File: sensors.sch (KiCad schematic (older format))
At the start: 13 parts

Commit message: Update schematic labels to handle hierarchical signal dependencies
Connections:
- wire segments 42 -> 48
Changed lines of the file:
@@
 	1    0    0    -1
 $EndComp
-Text Label 3750 1950 0    39   ~ 0
-SPI1_MISO
-Text Label 3750 2100 0    39   ~ 0
-SPI1_NSS
-Text Label 3750 1800 0    39   ~ 0
-SPI1_MOSI
-Text Label 3750 1700 0    39   ~ 0
-SPI1_SCK
 NoConn ~ 3700 1450
 NoConn ~ 3700 1550
 NoConn ~ 3700 2450
-Text Label 3750 2250 0    39   ~ 0
-MPU9250_INT
 $Comp
 L MPU-9250 U?
@@
 	1    0    0    -1
 $EndComp
-Text Label 5900 1600 2    39   ~ 0
-+2.8V
-Text Label 5900 2150 2    39   ~ 0
-+2.8V
 Wire Wire Line
 	2100 2800 1900 2800
@@
 	1900 2800 1900 2850
 Wire Wire Line
-	1650 1450 2100 1450
+	1650 1450 2050 1450
+Wire Wire Line
+	2050 1450 2100 1450
 Wire Wire Line
 	1650 1750 2100 1750
@@
 	3700 2700 3850 2700
 Wire Wire Line
-	5900 1600 6200 1600
-Wire Wire Line
-	5900 2150 6200 2150
+	5900 1600 6050 1600
+Wire Wire Line
+	6050 1600 6200 1600
+Wire Wire Line
+	5900 2150 6050 2150
+Wire Wire Line
+	6050 2150 6200 2150
 $Comp
 L C C?
@@
 	1    0    0    -1
 $EndComp
-Text Label 7950 1150 0    39   ~ 0
-+2.8V
-Wire Wire Line
-	7700 1150 7950 1150
+Wire Wire Line
+	7700 1150 7850 1150
+Wire Wire Line
+	7850 1150 7950 1150
 Wire Wire Line
 	7850 1150 7850 1250
@@
 Wire Wire Line
 	7850 1700 7850 1550
-Text Label 9300 1050 0    39   ~ 0
-+2.8V
 $Comp
 L R R?
@@
 	9200 1400 9200 1050
 Wire Wire Line
-	9050 1050 9300 1050
+	9050 1050 9200 1050
+Wire Wire Line
+	9200 1050 9300 1050
 Wire Wire Line
 	9050 1050 9050 1100
@@
 	10150 1600 10150 1550
 Wire Wire Line
-	10150 1550 10400 1550
+	10150 1550 10300 1550
+Wire Wire Line
+	10300 1550 10400 1550
 Wire Wire Line
 	10300 1550 10300 1900
@@
 Connection ~ 10150 2200
 Connection ~ 10300 1550
-Text Label 10400 1550 0    39   ~ 0
-+2.8V
-Text Label 9500 1700 0    39   ~ 0
+Wire Wire Line
+	9500 1700 9450 1700
+Wire Wire Line
+	10600 2200 10550 2200
+Text HLabel 3750 1700 2    39   Input ~ 0
+SPI1_SCK
+Text HLabel 3750 1800 2    39   Input ~ 0
+SPI1_MOSI
+Text HLabel 3750 1950 2    39   Input ~ 0
+SPI1_MISO
+Text HLabel 3750 2100 2    39   Input ~ 0
+SPI1_NSS
+Text HLabel 3750 2250 2    39   Input ~ 0
+MPU9250_INT
+Text HLabel 5900 1600 0    39   Input ~ 0
++2.8V
+Text HLabel 5900 2150 0    39   Input ~ 0
++2.8V
+Text HLabel 7950 1150 2    39   Input ~ 0
++2.8V
+Text HLabel 9300 1050 2    39   Input ~ 0
++2.8V
+Text HLabel 10400 1550 2    39   Input ~ 0
++2.8V
+Text HLabel 10600 2200 2    39   Input ~ 0
+I2C1_SDA
+Text HLabel 9500 1700 2    39   Input ~ 0
 I2C1_SCL
-Wire Wire Line
-	9500 1700 9450 1700
-Text Label 10600 2200 0    39   ~ 0
-I2C1_SDA
-Wire Wire Line
-	10600 2200 10550 2200
 $EndSCHEMATC

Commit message: Add principal power supply
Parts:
- removed Q? (x2): BSS138, SOT-23, symbol BSS138
- removed R? (x2): 2.2k, symbol R
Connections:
- net labels removed: +2.8V, I2C1_SCL_2.8V, I2C1_SDA_2.8V
- wire segments 48 -> 32
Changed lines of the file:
@@
 	1900 2800 1900 2850
 Wire Wire Line
-	1650 1450 2050 1450
-Wire Wire Line
-	2050 1450 2100 1450
+	1650 1450 2100 1450
 Wire Wire Line
 	1650 1750 2100 1750
@@
 	3700 2700 3850 2700
 Wire Wire Line
-	5900 1600 6050 1600
+	5900 1600 6200 1600
 Wire Wire Line
-	6050 1600 6200 1600
-Wire Wire Line
-	5900 2150 6050 2150
-Wire Wire Line
-	6050 2150 6200 2150
+	5900 2150 6200 2150
 $Comp
 L C C?
@@
 	7700 1150 7850 1150
 Wire Wire Line
-	7850 1150 7950 1150
-Wire Wire Line
-	7850 1150 7850 1250
+	7850 1100 7850 1250
 Wire Wire Line
 	7700 1150 7700 1250
@@
 Wire Wire Line
 	7850 1700 7850 1550
-$Comp
-L R R?
-U 1 1 5536FF70
-P 10150 1750
-F 0 "R?" V 10230 1750 50  0000 C CNN
-F 1 "2.2k" V 10150 1750 50  0000 C CNN
-F 2 "" V 10080 1750 30  0000 C CNN
-F 3 "" H 10150 1750 30  0000 C CNN
-	1    10150 1750
-	1    0    0    -1
-$EndComp
 Wire Wire Line
 	7650 1850 7700 1850
@@
 	7700 1600 7700 1550
 Text Label 7700 1850 0    39   ~ 0
-I2C1_SCL_2.8V
+I2C1_SCL
 Text Label 7700 1950 0    39   ~ 0
-I2C1_SDA_2.8V
+I2C1_SDA
 $Comp
 L VL6180X U?
@@
 	1    0    0    -1
 $EndComp
-$Comp
-L R R?
-U 1 1 5536FEA0
-P 9050 1250
-F 0 "R?" V 9130 1250 50  0000 C CNN
-F 1 "2.2k" V 9050 1250 50  0000 C CNN
-F 2 "" V 8980 1250 30  0000 C CNN
-F 3 "" H 9050 1250 30  0000 C CNN
-	1    9050 1250
-	1    0    0    -1
-$EndComp
-$Comp
-L BSS138 Q?
-U 1 1 5537886E
-P 9250 1600
-F 0 "Q?" H 9450 1675 50  0000 L CNN
-F 1 "BSS138" H 9450 1600 50  0000 L CNN
-F 2 "SOT-23" H 9450 1525 50  0000 L CIN
-F 3 "" H 9250 1600 50  0000 L CNN
-	1    9250 1600
-	0    1    1    0
-$EndComp
-$Comp
-L BSS138 Q?
-U 1 1 553788BF
-P 10350 2100
-F 0 "Q?" H 10550 2175 50  0000 L CNN
-F 1 "BSS138" H 10550 2100 50  0000 L CNN
-F 2 "SOT-23" H 10550 2025 50  0000 L CIN
-F 3 "" H 10350 2100 50  0000 L CNN
-	1    10350 2100
-	0    1    1    0
-$EndComp
-Text Label 9000 1700 2    39   ~ 0
-I2C1_SCL_2.8V
-Text Label 10100 2200 2    39   ~ 0
-I2C1_SDA_2.8V
-Wire Wire Line
-	9000 1700 9050 1700
-Wire Wire Line
-	10100 2200 10150 2200
-Wire Wire Line
-	9050 1700 9050 1400
-Connection ~ 9050 1700
-Wire Wire Line
-	9200 1400 9200 1050
-Wire Wire Line
-	9050 1050 9200 1050
-Wire Wire Line
-	9200 1050 9300 1050
-Wire Wire Line
-	9050 1050 9050 1100
-Connection ~ 9200 1050
-Wire Wire Line
-	10150 1600 10150 1550
-Wire Wire Line
-	10150 1550 10300 1550
-Wire Wire Line
-	10300 1550 10400 1550
-Wire Wire Line
-	10300 1550 10300 1900
-Wire Wire Line
-	10150 2200 10150 1900
-Connection ~ 10150 2200
-Connection ~ 10300 1550
-Wire Wire Line
-	9500 1700 9450 1700
-Wire Wire Line
-	10600 2200 10550 2200
 Text HLabel 3750 1700 2    39   Input ~ 0
 SPI1_SCK
@@
 Text HLabel 3750 2250 2    39   Input ~ 0
 MPU9250_INT
-Text HLabel 5900 1600 0    39   Input ~ 0
-+2.8V
-Text HLabel 5900 2150 0    39   Input ~ 0
-+2.8V
-Text HLabel 7950 1150 2    39   Input ~ 0
-+2.8V
-Text HLabel 9300 1050 2    39   Input ~ 0
-+2.8V
-Text HLabel 10400 1550 2    39   Input ~ 0
-+2.8V
-Text HLabel 10600 2200 2    39   Input ~ 0
-I2C1_SDA
-Text HLabel 9500 1700 2    39   Input ~ 0
-I2C1_SCL
+$Comp
+L VCC #PWR?
+U 1 1 55382F10
+P 7850 1100
+F 0 "#PWR?" H 7850 950 50  0001 C CNN
+F 1 "VCC" H 7850 1250 50  0000 C CNN
+F 2 "" H 7850 1100 60  0000 C CNN
+F 3 "" H 7850 1100 60  0000 C CNN
+	1    7850 1100
+	1    0    0    -1
+$EndComp
+$Comp
+L VCC #PWR?
+U 1 1 55382F46
+P 5900 1550
+F 0 "#PWR?" H 5900 1400 50  0001 C CNN
+F 1 "VCC" H 5900 1700 50  0000 C CNN
+F 2 "" H 5900 1550 60  0000 C CNN
+F 3 "" H 5900 1550 60  0000 C CNN
+	1    5900 1550
+	1    0    0    -1
+$EndComp
+$Comp
+L VCC #PWR?
+U 1 1 55382F63
+P 5900 2100
+F 0 "#PWR?" H 5900 1950 50  0001 C CNN
+F 1 "VCC" H 5900 2250 50  0000 C CNN
+F 2 "" H 5900 2100 60  0000 C CNN
+F 3 "" H 5900 2100 60  0000 C CNN
+	1    5900 2100
+	1    0    0    -1
+$EndComp
+Wire Wire Line
+	5900 2100 5900 2150
+Wire Wire Line
+	5900 1550 5900 1600
 $EndSCHEMATC

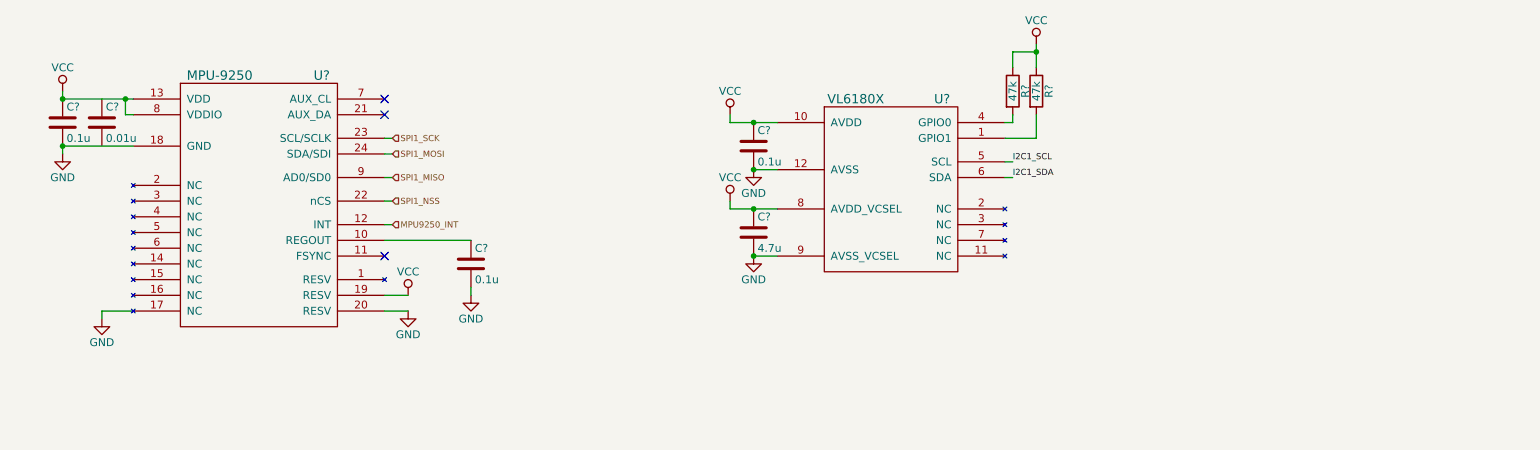
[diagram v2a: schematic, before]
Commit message: Barometer in schematic
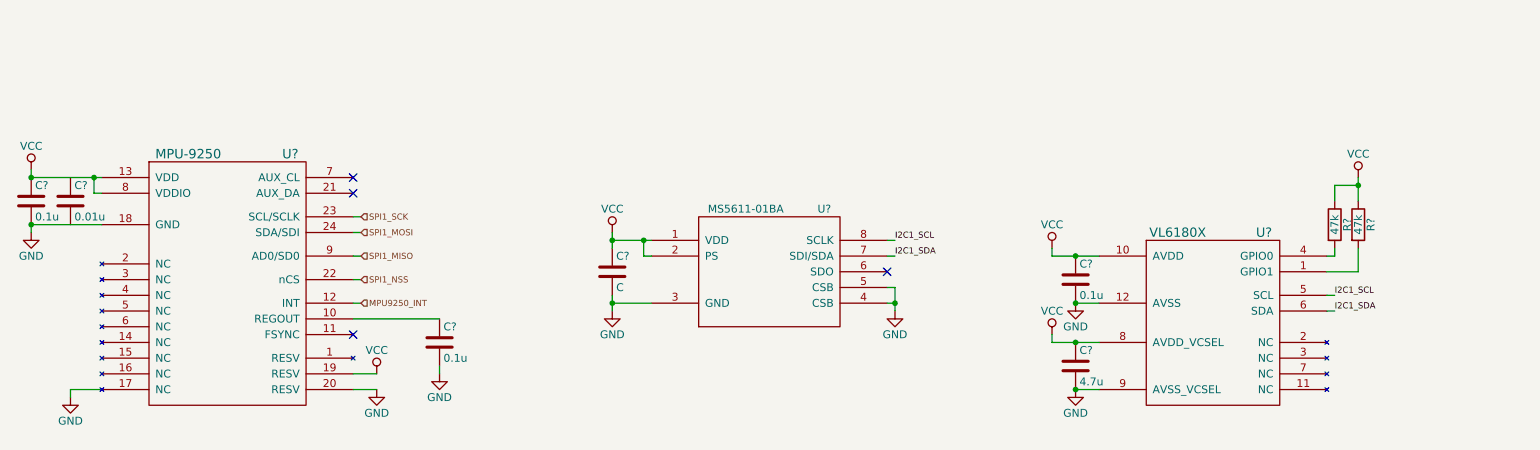
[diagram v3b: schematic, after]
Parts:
- added C?: C, symbol C
- added U?: MS5611-01BA, MODULE, symbol MS5611-01BA
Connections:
- net GND: now also C?.2, U?.3 (GND), U?.4 (CSB), U?.5 (CSB)
- net I2C1_SCL: now also U?.8 (SCLK)
- net I2C1_SDA: now also U?.7 (SDI/SDA)
- net VCC: now also C?.1, U?.1 (VDD), U?.2 (PS)
- no-connect marks 3 -> 4
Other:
- moved on the sheet: C?, R?, U?

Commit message: CAN transceiver added in schematics
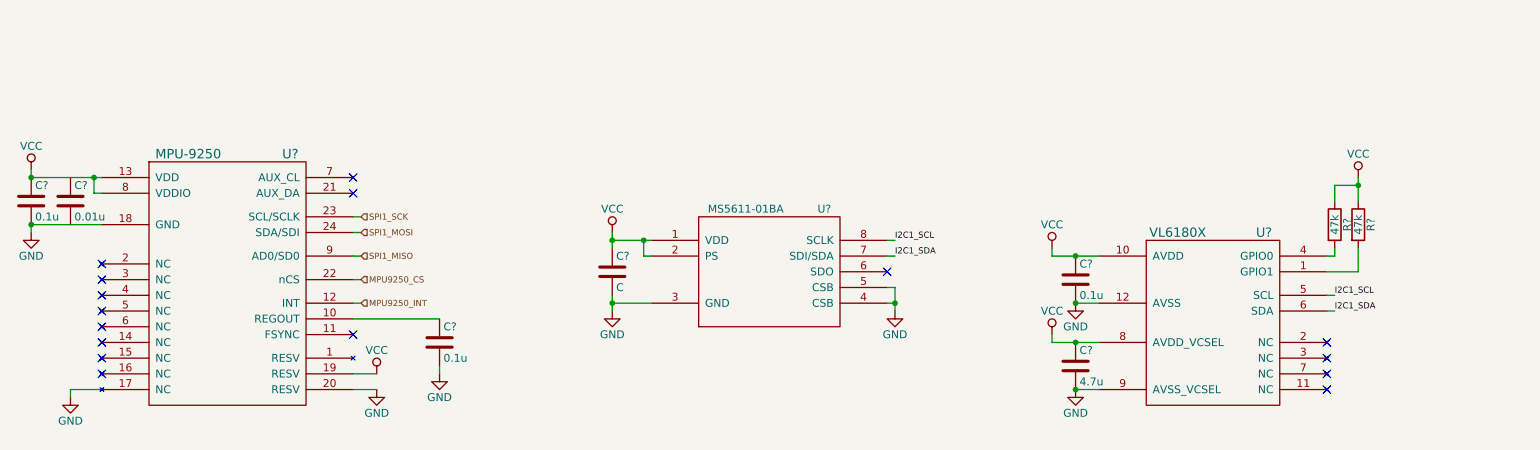
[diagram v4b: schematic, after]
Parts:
- removed U?: MPU-9250, symbol MPU-9250
- added U?: MPU-9250, symbol MPU-9250
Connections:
- net GND: now also U?.17 (NC), U?.18 (GND), U?.20 (RESV)
- net MPU9250_INT: now also U?.12 (INT)
- net SPI1_MISO: now also U?.9 (AD0/SD0)
- net SPI1_MOSI: now also U?.24 (SDA/SDI)
- net SPI1_SCK: now also U?.23 (SCL/SCLK)
- net VCC: now also U?.13 (VDD), U?.19 (RESV), U?.8 (VDDIO)
- net at C?.1: now also U?.10 (REGOUT)
- new net MPU9250_CS: U?.22 (nCS)
- no-connect marks 4 -> 16
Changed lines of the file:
@@
 NoConn ~ 3500 2950
-$Comp
-L MPU-9250 U?
-U 1 1 5536DEAA
-P 2700 2600
-F 0 "U?" H 3100 3400 60  0000 C CNN
-F 1 "MPU-9250" H 2450 3400 60  0000 C CNN
-F 2 "" H 2700 3200 60  0000 C CNN
-F 3 "" H 2700 3200 60  0000 C CNN
-	1    2700 2600
-	1    0    0    -1
-$EndComp
 $Comp
 L VCC #PWR?
@@
 SPI1_MISO
 Text HLabel 3550 2600 2    39   Input ~ 0
-SPI1_NSS
+MPU9250_CS
 Text HLabel 3550 2750 2    39   Input ~ 0
 MPU9250_INT
@@
 	6950 2650 6900 2650
 Connection ~ 6950 2750
+NoConn ~ 9700 3000
+NoConn ~ 9700 3100
+NoConn ~ 9700 3200
+NoConn ~ 9700 3300
+NoConn ~ 1900 3200
+NoConn ~ 1900 3100
+NoConn ~ 1900 3000
+NoConn ~ 1900 2900
+NoConn ~ 1900 2800
+NoConn ~ 1900 2700
+NoConn ~ 1900 2600
+NoConn ~ 1900 2500
+$Comp
+L MPU-9250 U?
+U 1 1 553B9407
+P 2700 2600
+F 0 "U?" H 3100 3400 60  0000 C CNN
+F 1 "MPU-9250" H 2450 3400 60  0000 C CNN
+F 2 "" H 2700 3200 60  0000 C CNN
+F 3 "" H 2700 3200 60  0000 C CNN
+	1    2700 2600
+	1    0    0    -1
+$EndComp
 $EndSCHEMATC

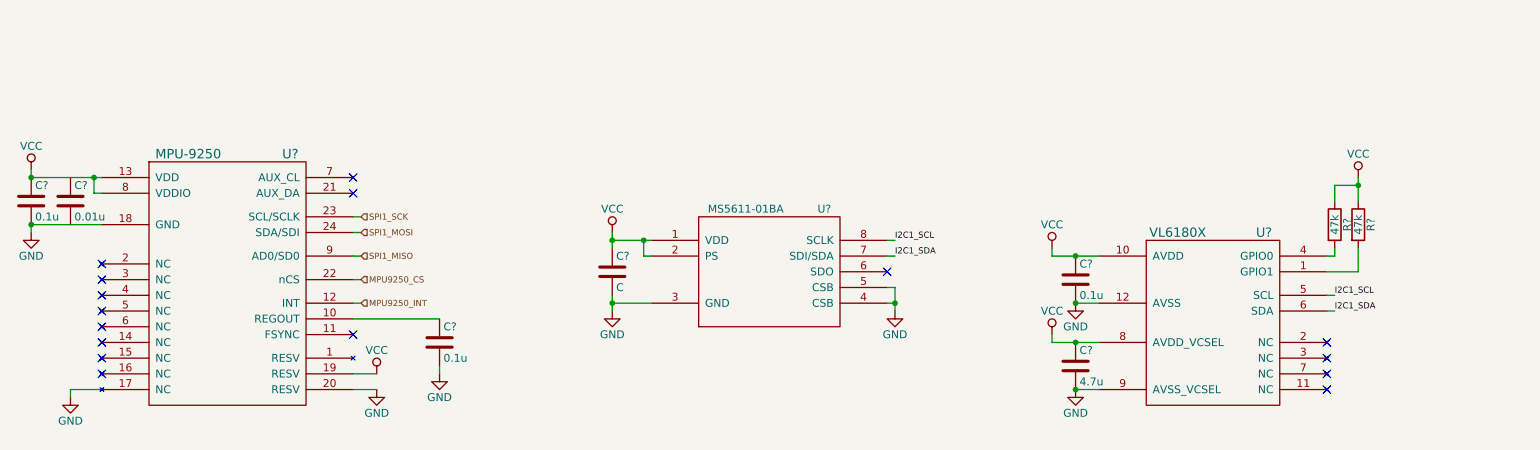
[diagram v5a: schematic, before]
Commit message: nRF24L01+ integrated + correct capacitors
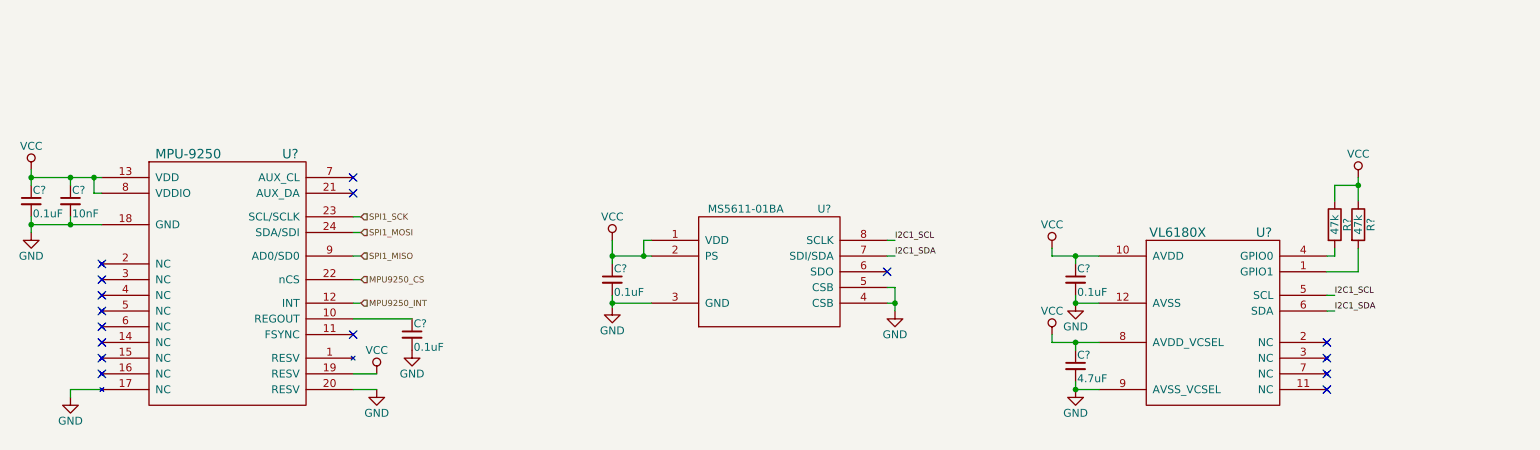
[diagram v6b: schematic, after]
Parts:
- removed C? (x3): 0.1u, symbol C
- removed C?: 0.01u, symbol C
- removed C?: 4.7u, symbol C
- removed C?: C, symbol C
- added C? (x4): 0.1uF, symbol C_Small
- added C?: 10nF, symbol C_Small
- added C?: 4.7uF, symbol C_Small
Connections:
- net GND: now also C?.2, C?.2, C?.2, C?.2, C?.2, C?.2
- net VCC: now also C?.1, C?.1, C?.1, C?.1, C?.1
- net at U?.10 (REGOUT): now also C?.1
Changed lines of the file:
@@
-$EndComp
-$Comp
-L C C?
-U 1 1 5536D1BC
-P 1450 2100
-F 0 "C?" H 1475 2200 50  0000 L CNN
-F 1 "0.1u" H 1475 2000 50  0000 L CNN
-F 2 "" H 1488 1950 30  0000 C CNN
-F 3 "" H 1450 2100 60  0000 C CNN
-	1    1450 2100
-	1    0    0    -1
 $EndComp
 $Comp
@@
 $EndComp
 $Comp
-L C C?
-U 1 1 5536D8E2
-P 1700 2100
-F 0 "C?" H 1725 2200 50  0000 L CNN
-F 1 "0.01u" H 1725 2000 50  0000 L CNN
-F 2 "" H 1738 1950 30  0000 C CNN
-F 3 "" H 1700 2100 60  0000 C CNN
-	1    1700 2100
-	1    0    0    -1
-$EndComp
-$Comp
-L C C?
-U 1 1 5536D99A
-P 4050 3000
-F 0 "C?" H 4075 3100 50  0000 L CNN
-F 1 "0.1u" H 4075 2900 50  0000 L CNN
-F 2 "" H 4088 2850 30  0000 C CNN
-F 3 "" H 4050 3000 60  0000 C CNN
-	1    4050 3000
-	1    0    0    -1
-$EndComp
-$Comp
 L GND #PWR?
 U 1 1 5536D9F2
-P 4050 3200
-F 0 "#PWR?" H 4050 2950 50  0001 C CNN
-F 1 "GND" H 4050 3050 50  0000 C CNN
-F 2 "" H 4050 3200 60  0000 C CNN
-F 3 "" H 4050 3200 60  0000 C CNN
-	1    4050 3200
+P 3875 3050
+F 0 "#PWR?" H 3875 2800 50  0001 C CNN
+F 1 "GND" H 3875 2900 50  0000 C CNN
+F 2 "" H 3875 3050 60  0000 C CNN
+F 3 "" H 3875 3050 60  0000 C CNN
+	1    3875 3050
 	1    0    0    -1
 $EndComp
@@
 	1450 2250 1900 2250
 Wire Wire Line
-	1450 1950 1450 1900
-Wire Wire Line
-	1450 2250 1450 2300
+	1450 1900 1450 2000
+Wire Wire Line
+	1450 2200 1450 2300
 Connection ~ 1450 2250
 Connection ~ 1450 1950
@@
 	1850 2050 1850 1950
 Wire Wire Line
-	4050 3200 4050 3150
-Wire Wire Line
-	4050 2850 3500 2850
+	3875 2850 3500 2850
 Wire Wire Line
 	3550 2450 3500 2450
@@
 	3500 3200 3650 3200
 Wire Wire Line
-	7950 2450 8250 2450
-Wire Wire Line
 	7950 3000 8250 3000
-$Comp
-L C C?
-U 1 1 5536FB84
-P 8100 3150
-F 0 "C?" H 8125 3250 50  0000 L CNN
-F 1 "4.7u" H 8125 3050 50  0000 L CNN
-F 2 "" H 8138 3000 30  0000 C CNN
-F 3 "" H 8100 3150 60  0000 C CNN
-	1    8100 3150
-	1    0    0    -1
-$EndComp
 Wire Wire Line
 	8100 3300 8250 3300
@@
 Connection ~ 8100 3300
 Connection ~ 8100 3000
-$Comp
-L C C?
-U 1 1 5536FC5F
-P 8100 2600
-F 0 "C?" H 8125 2700 50  0000 L CNN
-F 1 "0.1u" H 8125 2500 50  0000 L CNN
-F 2 "" H 8138 2450 30  0000 C CNN
-F 3 "" H 8100 2600 60  0000 C CNN
-	1    8100 2600
-	1    0    0    -1
-$EndComp
-Wire Wire Line
-	8250 2750 8100 2750
-Connection ~ 8100 2750
-Connection ~ 8100 2450
 $Comp
 L R R?
@@
 $EndComp
 $Comp
-L C C?
-U 1 1 5538644F
-P 5150 2550
-F 0 "C?" H 5175 2650 50  0000 L CNN
-F 1 "C" H 5175 2450 50  0000 L CNN
-F 2 "" H 5188 2400 30  0000 C CNN
-F 3 "" H 5150 2550 60  0000 C CNN
-	1    5150 2550
-	1    0    0    -1
-$EndComp
-$Comp
 L VCC #PWR?
 U 1 1 553864D9
-P 5150 2300
-F 0 "#PWR?" H 5150 2150 50  0001 C CNN
-F 1 "VCC" H 5150 2450 50  0000 C CNN
-F 2 "" H 5150 2300 60  0000 C CNN
-F 3 "" H 5150 2300 60  0000 C CNN
-	1    5150 2300
+P 5150 2350
+F 0 "#PWR?" H 5150 2200 50  0001 C CNN
+F 1 "VCC" H 5150 2500 50  0000 C CNN
+F 2 "" H 5150 2350 60  0000 C CNN
+F 3 "" H 5150 2350 60  0000 C CNN
+	1    5150 2350
 	1    0    0    -1
 $EndComp
@@
 L GND #PWR?
 U 1 1 553864F8
-P 5150 2800
-F 0 "#PWR?" H 5150 2550 50  0001 C CNN
-F 1 "GND" H 5150 2650 50  0000 C CNN
-F 2 "" H 5150 2800 60  0000 C CNN
-F 3 "" H 5150 2800 60  0000 C CNN
-	1    5150 2800
-	1    0    0    -1
-$EndComp
-Wire Wire Line
-	5150 2700 5150 2800
+P 5150 2775
+F 0 "#PWR?" H 5150 2525 50  0001 C CNN
+F 1 "GND" H 5150 2625 50  0000 C CNN
+F 2 "" H 5150 2775 60  0000 C CNN
+F 3 "" H 5150 2775 60  0000 C CNN
+	1    5150 2775
+	1    0    0    -1
+$EndComp
+Wire Wire Line
+	5150 2700 5150 2775
 Wire Wire Line
 	5150 2750 5400 2750
 Connection ~ 5150 2750
 Wire Wire Line
-	5400 2350 5150 2350
-Wire Wire Line
-	5150 2300 5150 2400
-Connection ~ 5150 2350
-Wire Wire Line
-	5400 2450 5350 2450
+	5350 2350 5400 2350
+Wire Wire Line
+	5150 2350 5150 2500
+Wire Wire Line
+	5150 2450 5400 2450
 Wire Wire Line
 	5350 2450 5350 2350
-Connection ~ 5350 2350
 Text Label 6950 2350 0    39   ~ 0
 I2C1_SCL
@@
 	1    0    0    -1
 $EndComp
+$Comp
+L C_Small C?
+U 1 1 554288B9
+P 1450 2100
+F 0 "C?" H 1460 2170 50  0000 L CNN
+F 1 "0.1uF" H 1460 2020 50  0000 L CNN
+F 2 "" H 1450 2100 60  0000 C CNN
+F 3 "" H 1450 2100 60  0000 C CNN
+	1    1450 2100
+	1    0    0    -1
+$EndComp
+$Comp
+L C_Small C?
+U 1 1 55428A44
+P 1700 2100
+F 0 "C?" H 1710 2170 50  0000 L CNN
+F 1 "10nF" H 1710 2020 50  0000 L CNN
+F 2 "" H 1700 2100 60  0000 C CNN
+F 3 "" H 1700 2100 60  0000 C CNN
+	1    1700 2100
+	1    0    0    -1
+$EndComp
+Wire Wire Line
+	1700 2200 1700 2250
+Connection ~ 1700 2250
+Wire Wire Line
+	1700 2000 1700 1950
+Connection ~ 1700 1950
+$Comp
+L C_Small C?
+U 1 1 55428B56
+P 3875 2950
+F 0 "C?" H 3885 3020 50  0000 L CNN
+F 1 "0.1uF" H 3885 2870 50  0000 L CNN
+F 2 "" H 3875 2950 60  0000 C CNN
+F 3 "" H 3875 2950 60  0000 C CNN
+	1    3875 2950
+	1    0    0    -1
+$EndComp
+$Comp
+L C_Small C?
+U 1 1 55428C9E
+P 5150 2600
+F 0 "C?" H 5160 2670 50  0000 L CNN
+F 1 "0.1uF" H 5160 2520 50  0000 L CNN
+F 2 "" H 5150 2600 60  0000 C CNN
+F 3 "" H 5150 2600 60  0000 C CNN
+	1    5150 2600
+	1    0    0    -1
+$EndComp
+Connection ~ 5150 2450
+Connection ~ 5350 2450
+$Comp
+L C_Small C?
+U 1 1 55429127
+P 8100 2600
+F 0 "C?" H 8110 2670 50  0000 L CNN
+F 1 "0.1uF" H 8110 2520 50  0000 L CNN
+F 2 "" H 8100 2600 60  0000 C CNN
+F 3 "" H 8100 2600 60  0000 C CNN
+	1    8100 2600
+	1    0    0    -1
+$EndComp
+Wire Wire Line
+	8250 2750 8100 2750
+Wire Wire Line
+	8100 2750 8100 2700
+Wire Wire Line
+	8100 2500 8100 2450
+Wire Wire Line
+	7950 2450 8250 2450
+Connection ~ 8100 2450
+Connection ~ 8100 2750
+$Comp
+L C_Small C?
+U 1 1 55429407
+P 8100 3150
+F 0 "C?" H 8110 3220 50  0000 L CNN
+F 1 "4.7uF" H 8110 3070 50  0000 L CNN
+F 2 "" H 8100 3150 60  0000 C CNN
+F 3 "" H 8100 3150 60  0000 C CNN
+	1    8100 3150
+	1    0    0    -1
+$EndComp
+Wire Wire Line
+	8100 3050 8100 3000
+Wire Wire Line
+	8100 3250 8100 3300
 $EndSCHEMATC
